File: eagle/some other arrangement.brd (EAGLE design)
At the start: 22 parts

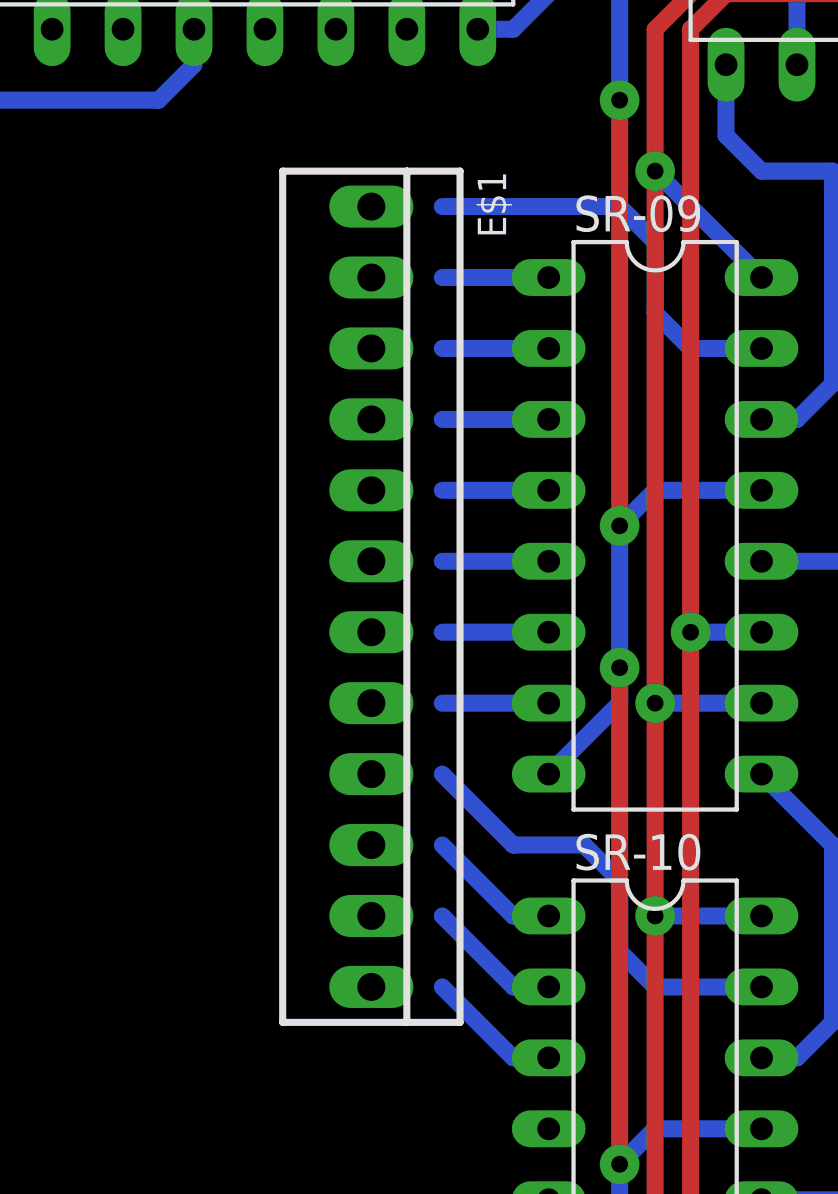
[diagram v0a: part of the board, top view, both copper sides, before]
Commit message: moved hours connectors
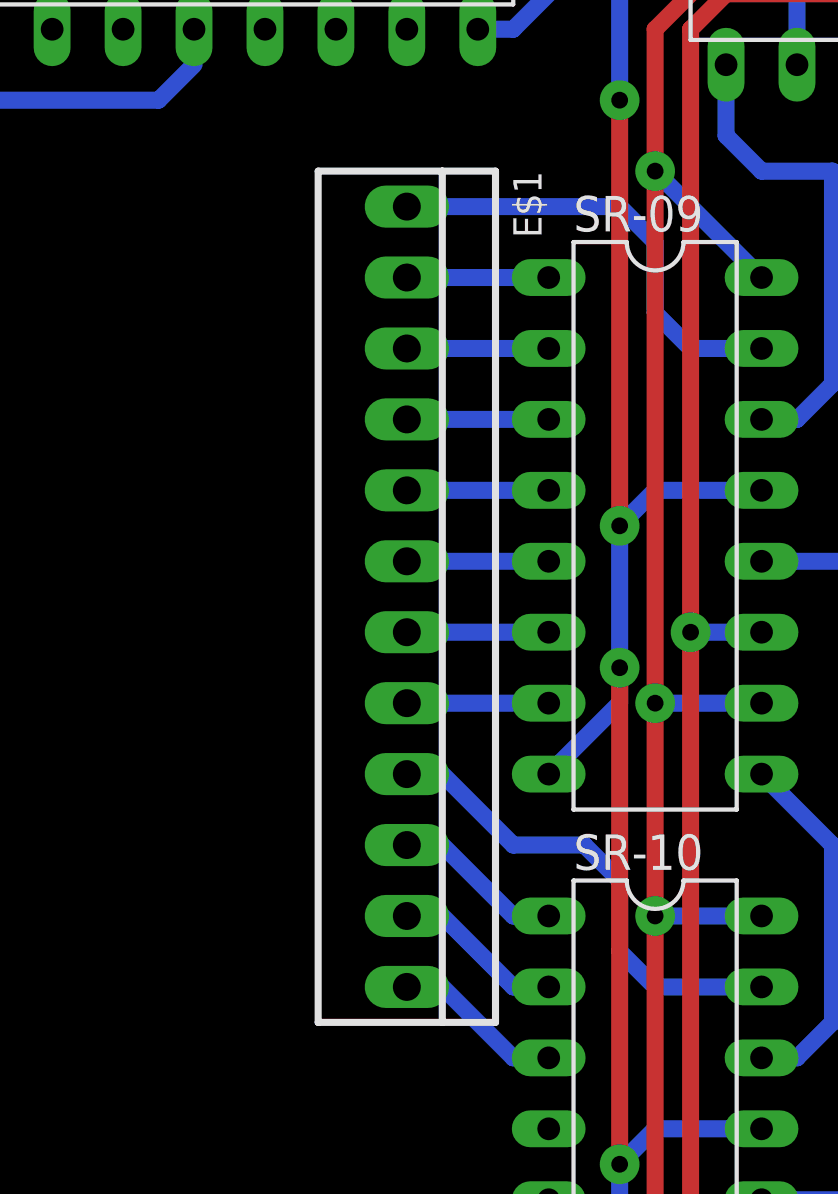
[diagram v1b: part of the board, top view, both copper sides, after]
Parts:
- moved E$1 1.27 mm to (57.1, 58.4)
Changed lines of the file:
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@@
 <element name="E$20" library="transistor-npn" package="TO92-BCE" value="" x="87.63" y="91.44"/>
 <element name="E$21" library="transistor-npn" package="TO92-BCE" value="" x="95.25" y="91.44"/>
-<element name="E$1" library="con-molex" package="22-23-2121" value="" x="55.88" y="58.42" rot="R270"/>
+<element name="E$1" library="con-molex" package="22-23-2121" value="" x="57.15" y="58.42" rot="R270"/>
 </elements>
 <signals>
